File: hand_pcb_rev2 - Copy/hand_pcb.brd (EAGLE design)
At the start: 65.2 x 60.5 mm, 66 parts

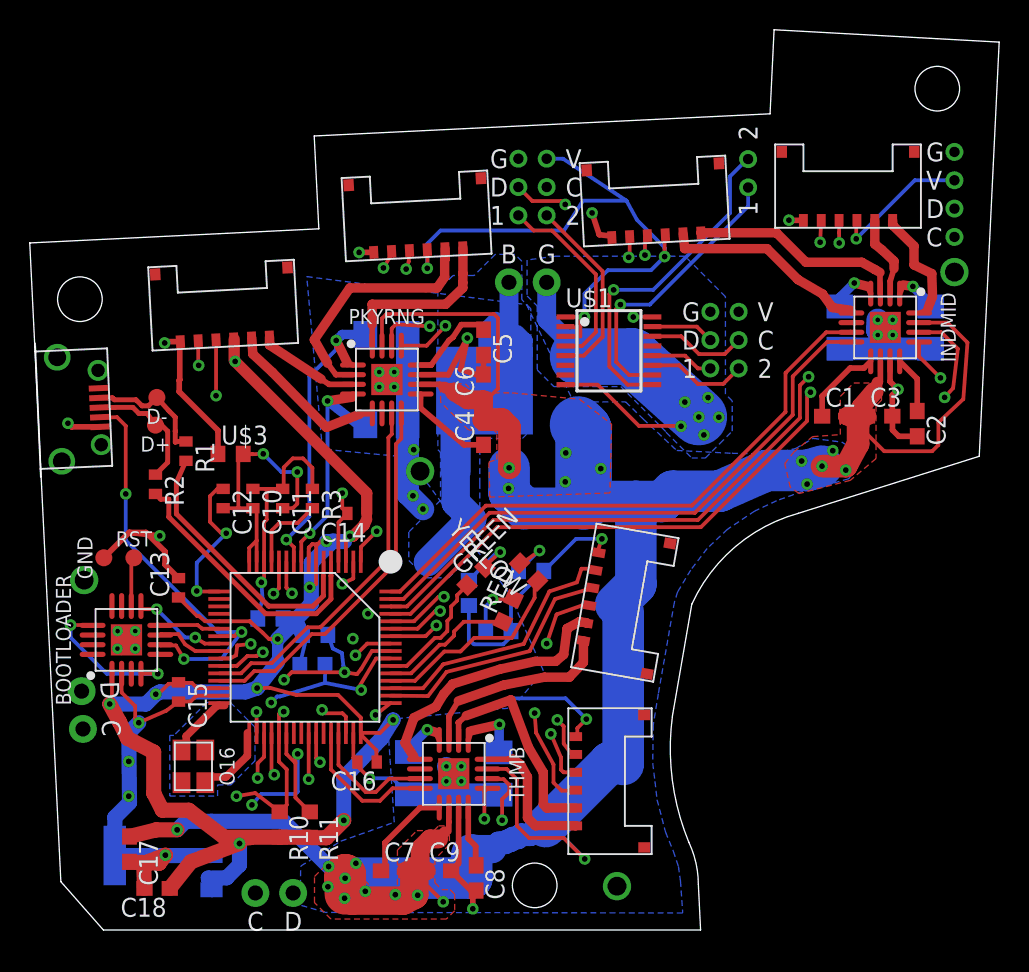
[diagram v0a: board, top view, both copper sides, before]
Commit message: added testpads for error pins on motor drivers
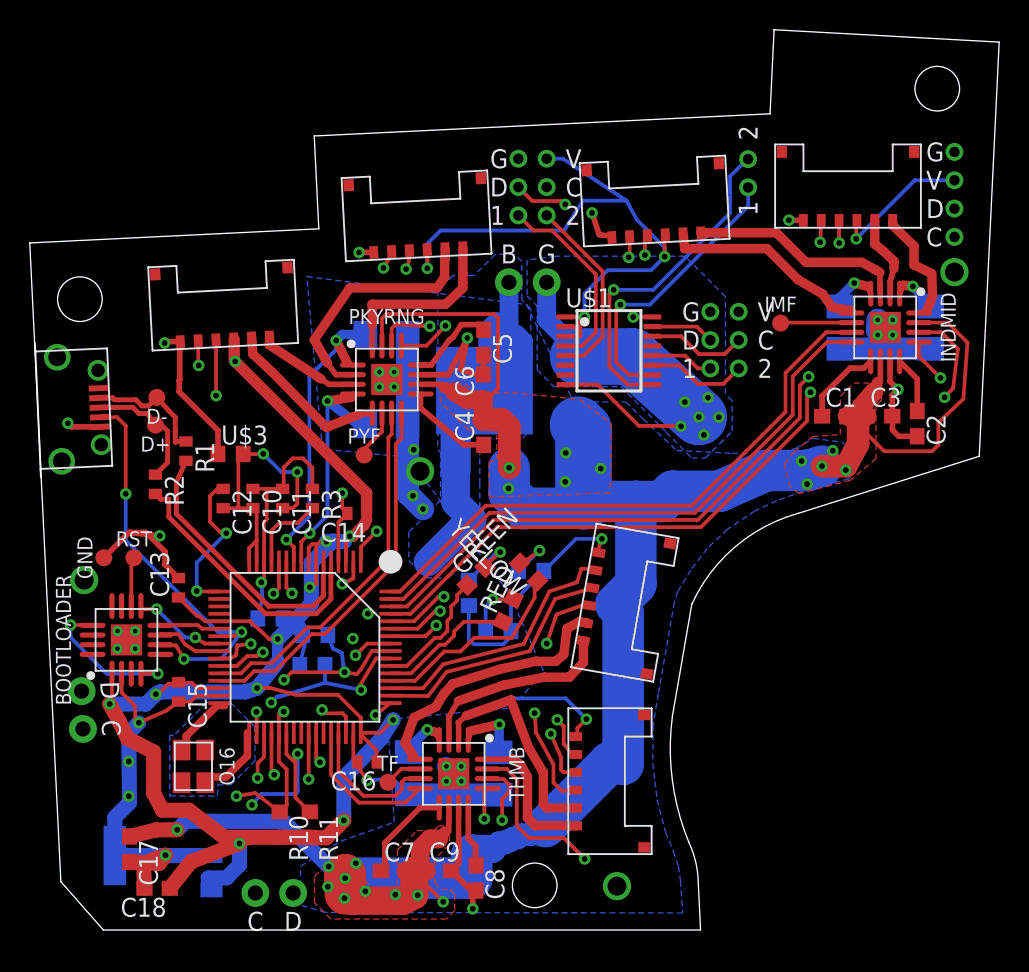
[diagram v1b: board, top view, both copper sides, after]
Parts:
- added IMF, PYF, TF: TESTPAD, 445-eagle-lib:TESTPAD
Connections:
- new net N$4: IMF.P$1, INDMID.6
- new net N$5: PKYRNG.6, PYF.P$1
- new net N$6: TF.P$1, THMB.6
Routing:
- net N$4: track 0.00 -> 4.77 mm
- net N$5: track 0.00 -> 3.29 mm
- net N$6: track 0.00 -> 2.52 mm
- net THBPWM1: track 8.76 -> 9.50 mm
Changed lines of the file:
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@@
 <element name="GND" library="445-eagle-lib" package="TESTPAD" value="TESTPAD" x="4.9784" y="25.019" locked="yes" rot="R90"/>
 <element name="U$2" library="445-eagle-lib" package="PG-TO-252-3" value="SPD15P10PLG" x="32.6644" y="36.2585" rot="MR270"/>
-<element name="R10" library="rcl" package="R0603" value="1k" x="16.8021" y="7.0866" rot="R270"/>
-<element name="R11" library="rcl" package="R0603" value="1k" x="18.8214" y="7.0866" rot="R270"/>
+<element name="R10" library="rcl" package="R0603" value="1k" x="16.8021" y="7.0866" locked="yes" rot="R270"/>
+<element name="R11" library="rcl" package="R0603" value="1k" x="18.8214" y="7.0866" locked="yes" rot="R270"/>
 <element name="R12" library="rcl" package="R0603" value="1k" x="18.9992" y="17.8054" locked="yes" rot="MR0"/>
 <element name="R13" library="rcl" package="R0603" value="1k" x="19.1897" y="19.8374" locked="yes" rot="MR0"/>
@@
 <element name="U$8" library="445-eagle-lib" package="PSENSE4" value="PSENSE4" x="62.1538" y="52.2986" locked="yes"/>
 <element name="U$9" library="445-eagle-lib" package="MIC39100" value="MIC391003.3" x="8.9662" y="5.0038" rot="MR270"/>
-<element name="C17" library="rcl" package="C0603" value="" x="6.7056" y="5.4356" rot="R270"/>
-<element name="C18" library="rcl" package="C0603" value="" x="8.5598" y="2.794" rot="R180"/>
-<element name="RED" library="445-eagle-lib" package="L0603" value="LED0603" x="32.1564" y="21.4884" rot="R65"/>
-<element name="GREEN" library="445-eagle-lib" package="L0603" value="LED0603" x="29.9974" y="23.7744" rot="R45"/>
-<element name="R14" library="rcl" package="R0603" value="100" x="31.496" y="20.0914" rot="MR180"/>
-<element name="R15" library="rcl" package="R0603" value="200" x="29.5148" y="22.6568" rot="MR270"/>
-<element name="R16" library="rcl" package="R0603" value="200" x="33.7058" y="24.13" rot="MR180"/>
-<element name="YELLOW" library="445-eagle-lib" package="L0603" value="LED0603" x="33.528" y="24.0538" rot="R135"/>
+<element name="C17" library="rcl" package="C0603" value="" x="6.7056" y="5.4356" locked="yes" rot="R270"/>
+<element name="C18" library="rcl" package="C0603" value="" x="8.5598" y="2.794" locked="yes" rot="R180"/>
+<element name="RED" library="445-eagle-lib" package="L0603" value="LED0603" x="32.1564" y="21.4884" locked="yes" rot="R65"/>
+<element name="GREEN" library="445-eagle-lib" package="L0603" value="LED0603" x="29.9974" y="23.7744" locked="yes" rot="R45"/>
+<element name="R14" library="rcl" package="R0603" value="100" x="31.496" y="20.0914" locked="yes" rot="MR180"/>
+<element name="R15" library="rcl" package="R0603" value="200" x="29.5148" y="22.6568" locked="yes" rot="MR270"/>
+<element name="R16" library="rcl" package="R0603" value="200" x="33.7058" y="24.13" locked="yes" rot="MR180"/>
+<element name="YELLOW" library="445-eagle-lib" package="L0603" value="LED0603" x="33.528" y="24.0538" locked="yes" rot="R135"/>
 <element name="U$10" library="445-eagle-lib" package="THRUHOLE2" value="THRUHOLE2" x="33.4772" y="43.5356"/>
 <element name="U$11" library="445-eagle-lib" package="THRUHOLEI2C" value="THRUHOLEI2C" x="16.4338" y="2.4892" rot="R180"/>
 <element name="U$12" library="445-eagle-lib" package="THRUHOLEI2C" value="THRUHOLEI2C" x="3.5306" y="14.7828" rot="R272"/>
+<element name="IMF" library="445-eagle-lib" package="TESTPAD" value="TESTPAD" x="50.4698" y="40.7924"/>
+<element name="PYF" library="445-eagle-lib" package="TESTPAD" value="TESTPAD" x="22.479" y="31.9278"/>
+<element name="TF" library="445-eagle-lib" package="TESTPAD" value="TESTPAD" x="24.0792" y="9.9314"/>
 </elements>
 <signals>
@@
 <wire x1="10.0043" y1="15.3543" x2="10" y2="15.35" width="0.254" layer="1"/>
 <wire x1="22.0238" y1="11.2892" x2="22.0238" y2="11.0089" width="0.254" layer="1"/>
-<wire x1="22.0238" y1="11.0089" x2="22.8346" y2="10.1981" width="0.254" layer="1"/>
-<via x="22.8346" y="10.1981" extent="1-16" drill="0.381"/>
-<wire x1="22.8346" y1="10.1981" x2="24.3717" y2="10.1981" width="0.254" layer="16"/>
+<wire x1="22.0238" y1="11.0089" x2="22.6822" y2="10.0457" width="0.254" layer="1"/>
+<via x="22.6822" y="10.0457" extent="1-16" drill="0.381"/>
+<wire x1="22.6822" y1="10.0457" x2="24.3717" y2="10.1981" width="0.254" layer="16"/>
 <wire x1="24.3717" y1="10.1981" x2="25.4508" y2="9.119" width="0.254" layer="16"/>
 <wire x1="36.8554" y1="38.5445" x2="40.4876" y2="38.5445" width="3.81" layer="16"/>
@@
 <contactref element="THMB" pad="8"/>
 <contactref element="HAND_MICRO" pad="44"/>
-<wire x1="20.25" y1="13.25" x2="20.25" y2="10.7888" width="0.254" layer="1"/>
-<wire x1="20.25" y1="10.7888" x2="22.352" y2="8.6868" width="0.254" layer="1"/>
-<wire x1="26.225" y1="9.525" x2="24.384" y2="9.525" width="0.254" layer="1"/>
-<wire x1="24.384" y1="9.525" x2="23.5458" y2="8.6868" width="0.254" layer="1"/>
-<wire x1="23.5458" y1="8.6868" x2="22.352" y2="8.6868" width="0.254" layer="1"/>
+<wire x1="26.225" y1="9.525" x2="25.2598" y2="8.5598" width="0.254" layer="1"/>
+<wire x1="25.2598" y1="8.5598" x2="22.1234" y2="8.5598" width="0.254" layer="1"/>
+<wire x1="22.1234" y1="8.5598" x2="20.25" y2="10.4332" width="0.254" layer="1"/>
+<wire x1="20.25" y1="10.4332" x2="20.25" y2="13.25" width="0.254" layer="1"/>
 </signal>
 <signal name="THBPWM1">
 <contactref element="THMB" pad="7"/>
 <contactref element="HAND_MICRO" pad="45"/>
-<wire x1="20.75" y1="13.25" x2="20.75" y2="11.1016" width="0.254" layer="1"/>
-<wire x1="20.75" y1="11.1016" x2="22.5806" y2="9.271" width="0.254" layer="1"/>
-<wire x1="26.225" y1="10.175" x2="24.1577" y2="10.175" width="0.254" layer="1"/>
-<wire x1="24.1577" y1="10.175" x2="23.2537" y2="9.271" width="0.254" layer="1"/>
-<wire x1="23.2537" y1="9.271" x2="22.5806" y2="9.271" width="0.254" layer="1"/>
+<wire x1="26.225" y1="10.175" x2="25.2372" y2="10.175" width="0.254" layer="1"/>
+<wire x1="25.2372" y1="10.175" x2="24.9936" y2="9.9314" width="0.254" layer="1"/>
+<wire x1="24.9936" y1="9.9314" x2="24.9936" y2="9.4234" width="0.254" layer="1"/>
+<wire x1="24.9936" y1="9.4234" x2="24.5872" y2="9.017" width="0.254" layer="1"/>
+<wire x1="24.5872" y1="9.017" x2="22.4282" y2="9.017" width="0.254" layer="1"/>
+<wire x1="22.4282" y1="9.017" x2="20.75" y2="10.6952" width="0.254" layer="1"/>
+<wire x1="20.75" y1="10.6952" x2="20.75" y2="13.25" width="0.254" layer="1"/>
 </signal>
 <signal name="THAPWM2">
@@
 <wire x1="33.9344" y1="23.258115625" x2="34.129040625" y2="23.45275625" width="0.254" layer="1"/>
 </signal>
+<signal name="N$4">
+<contactref element="INDMID" pad="6"/>
+<contactref element="IMF" pad="P$1"/>
+<wire x1="55.225" y1="40.825" x2="50.5024" y2="40.825" width="0.254" layer="1"/>
+<wire x1="50.5024" y1="40.825" x2="50.4698" y2="40.7924" width="0.254" layer="1"/>
+</signal>
+<signal name="N$5">
+<contactref element="PKYRNG" pad="6"/>
+<contactref element="PYF" pad="P$1"/>
+<wire x1="23.675" y1="34.725" x2="23.675" y2="33.5048" width="0.254" layer="1"/>
+<wire x1="23.675" y1="33.5048" x2="22.479" y2="32.3088" width="0.254" layer="1"/>
+<wire x1="22.479" y1="32.3088" x2="22.479" y2="31.9278" width="0.254" layer="1"/>
+</signal>
+<signal name="N$6">
+<contactref element="TF" pad="P$1"/>
+<contactref element="THMB" pad="6"/>
+<wire x1="26.225" y1="10.825" x2="24.9728" y2="10.825" width="0.254" layer="1"/>
+<wire x1="24.9728" y1="10.825" x2="24.0792" y2="9.9314" width="0.254" layer="1"/>
+</signal>
 </signals>

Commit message: added .1uF cap for io expander for stability - not fully needed but good practice
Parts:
- added C19: 0.1, rcl:C0402
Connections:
- net +3V3: now also C19.1
- net GND: now also C19.2
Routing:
- net GND: track 413.7 -> 417.2 mm
- net +3V3: track 242.1 -> 244.5 mm
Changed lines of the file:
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@@
 <element name="PYF" library="445-eagle-lib" package="TESTPAD" value="TESTPAD" x="22.479" y="31.9278"/>
 <element name="TF" library="445-eagle-lib" package="TESTPAD" value="TESTPAD" x="24.0792" y="9.9314"/>
+<element name="C19" library="rcl" package="C0402" value="0.1" x="33.6804" y="38.9128" rot="R270"/>
 </elements>
 <signals>
@@
 <vertex x="35.3314" y="45.2882"/>
 </polygon>
+<contactref element="C19" pad="2"/>
+<wire x1="33.6804" y1="38.2628" x2="33.6804" y2="37.338" width="0.254" layer="1"/>
+<wire x1="33.6804" y1="37.338" x2="34.3625" y2="36.6559" width="0.254" layer="1"/>
+<wire x1="34.3625" y1="36.6559" x2="36.0049" y2="36.6559" width="0.254" layer="1"/>
 </signal>
 <signal name="+3V3">
@@
 <wire x1="15.28150625" y1="16.26529375" x2="15.28150625" y2="16.2602125" width="0.254" layer="1"/>
 <via x="15.28150625" y="16.2602125" extent="1-16" drill="0.381"/>
+<contactref element="C19" pad="1"/>
+<wire x1="36.0049" y1="39.9059" x2="34.0235" y2="39.9059" width="0.254" layer="1"/>
+<wire x1="34.0235" y1="39.9059" x2="33.6804" y2="39.5628" width="0.254" layer="1"/>
 <wire x1="13.0674" y1="6.2366" x2="14.0716" y2="6.1468" width="0" layer="19" extent="1-1"/>
 </signal>
